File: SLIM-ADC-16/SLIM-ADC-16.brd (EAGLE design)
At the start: 30.5 x 30.5 mm, 34 parts, among them J1 COAX, J2 COAX, P1 CONN-6PIN, Q1 MUN2211, Q2 MUN2211, SW1 SPDT-CONN, SW2 SPDT-CONN, U1 78L05, U2 AD7685, U3 AD7685

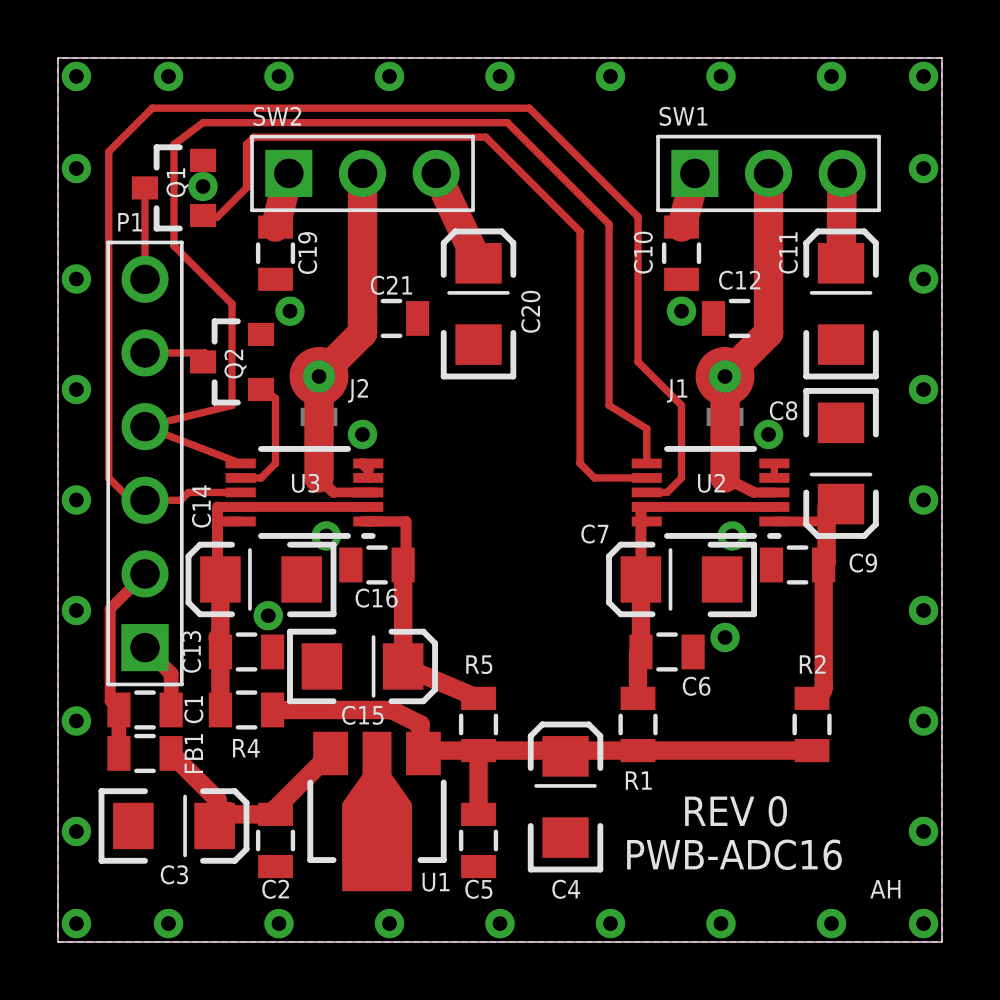
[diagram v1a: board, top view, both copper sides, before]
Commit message: Final changes for SLIM-ADC-16 before sending off to fab.
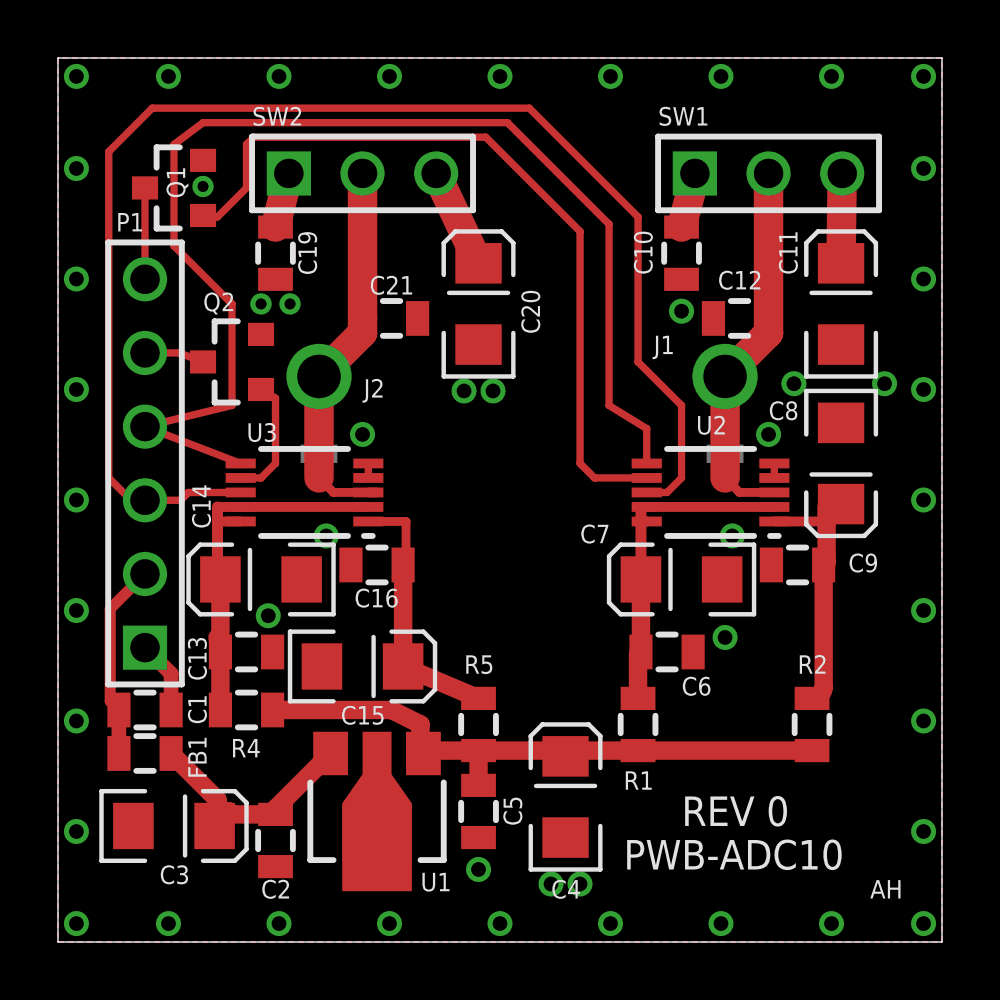
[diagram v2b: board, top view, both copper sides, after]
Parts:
- moved C5 1.00 mm to (14.5, 4.50)
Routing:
- net +5AD: track 22.0 -> 21.1 mm
- net GND: track 3.91 -> 3.82 mm, vias 41 -> 49
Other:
- board text added: "+10V"
- board text added: "2012/12/4"
- board text added: "CLK"
- board text added: "CONV"
- board text added: "GND"
- board text added: "MAG"
- board text added: "MDAT"
- board text added: "PDAT"
- board text added: "PHASE"
- board text added: "PWB-ADC10"
- board text added: "SLIM-ADC-16"
- board text removed: "PWB-ADC16"
